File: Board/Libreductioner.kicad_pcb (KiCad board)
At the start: 2 copper layers, 50.2 x 73 mm, 46 parts, among them J1 Conn_01x02_Male, J2 Conn_01x02_Male, J3 Conn_01x02_Male, J4 Conn_01x02_Male, J5 Conn_01x02_Male, J6 Conn_01x02_Male, Q1 IRF3205, U1 ATMEGA168A-AU, U2 PC817, U3 PC817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

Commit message: Added gerber files for production
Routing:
- net VCC: track 147.9 -> 151.9 mm
- net GND: track 482.3 -> 480.1 mm
- net /RESET: track 53.6 -> 55.6 mm

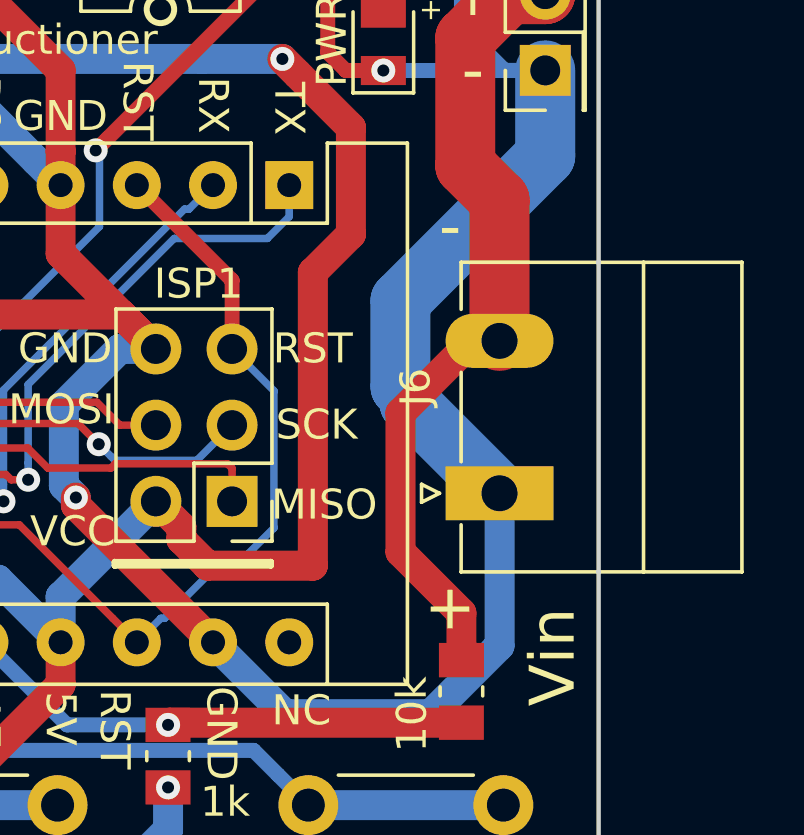
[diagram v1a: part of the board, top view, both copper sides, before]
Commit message: Fixed wrong description on Power Plug
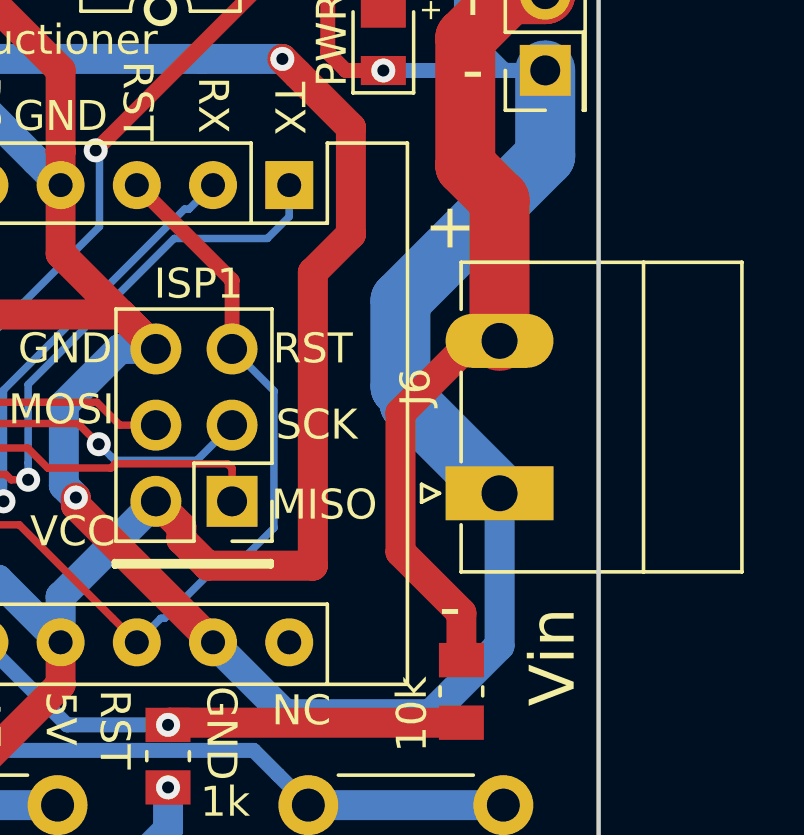
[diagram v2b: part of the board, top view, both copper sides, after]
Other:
- board text added: "Rev. 1.0.1 22.05.2018 Andreas Butti"
- board text removed: "Rev. 1.0 13.05.2018 Andreas Butti"
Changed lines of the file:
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@@
-(kicad_pcb (version 20171130) (host pcbnew 5.0.0-rc2-dev-unknown-f73b9a5~65~ubuntu16.04.1)
+(kicad_pcb (version 20171130) (host pcbnew 5.0.0-rc2-unknown-2d812c2~65~ubuntu16.04.1)
   (general
     (thickness 1.6)
@@
     (effects (font (size 0.8 0.8) (thickness 0.1)) (justify left))
   )
-  (gr_text "Rev. 1.0\n13.05.2018\nAndreas Butti" (at 89.535 79.756) (layer B.SilkS)
+  (gr_text "Rev. 1.0.1\n22.05.2018\nAndreas Butti" (at 89.535 79.756) (layer B.SilkS)
     (effects (font (size 1.5 1.5) (thickness 0.3)) (justify mirror))
   )
@@
   (gr_line (start 118.11 80.137) (end 118.11 70.104) (layer Edge.Cuts) (width 0.15))
   (gr_line (start 67.945 80.137) (end 67.945 67.945) (layer Edge.Cuts) (width 0.15))
-  (gr_text - (at 113.157 111.252) (layer F.SilkS)
+  (gr_text - (at 113.157 123.952) (layer F.SilkS)
     (effects (font (size 1.5 1.5) (thickness 0.3)))
   )
-  (gr_text + (at 113.157 123.952) (layer F.SilkS)
+  (gr_text + (at 113.157 111.252) (layer F.SilkS)
     (effects (font (size 1.5 1.5) (thickness 0.3)))
   )

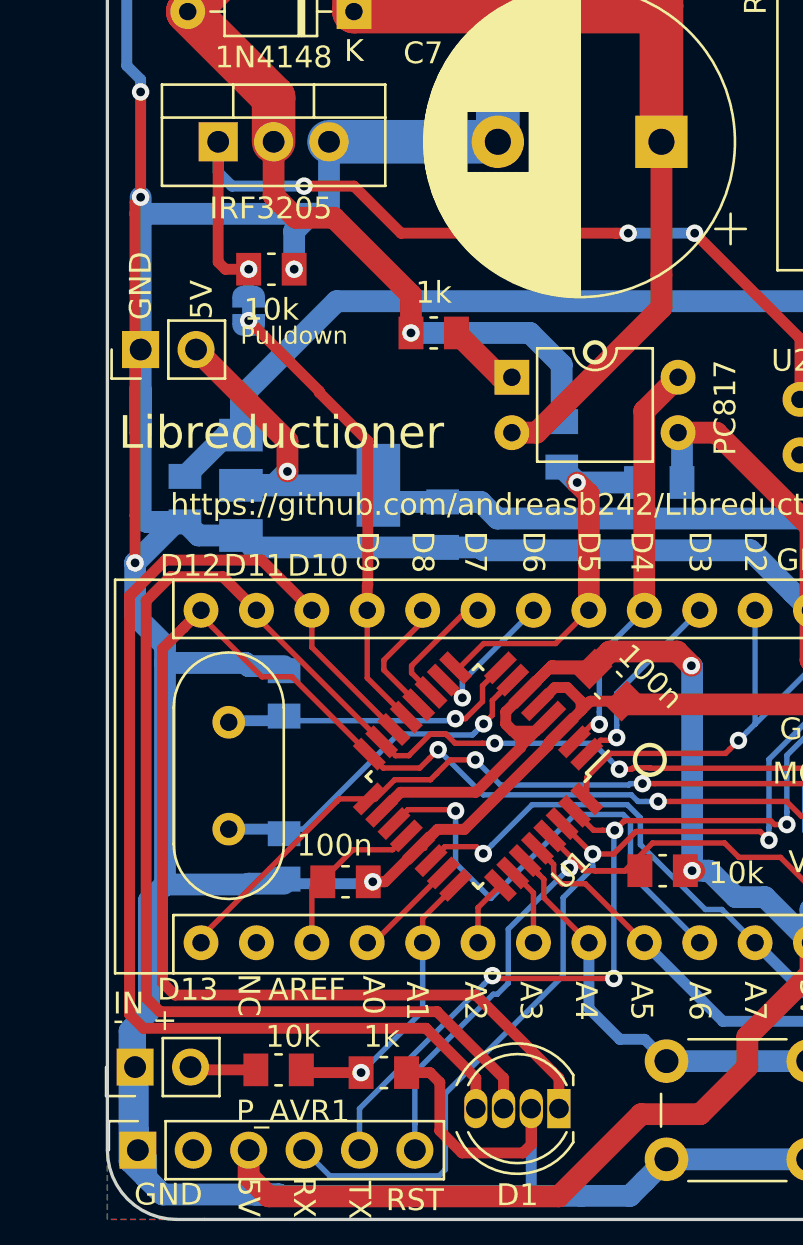
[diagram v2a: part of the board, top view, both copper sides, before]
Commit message: Fixed layout bugs found on Testing
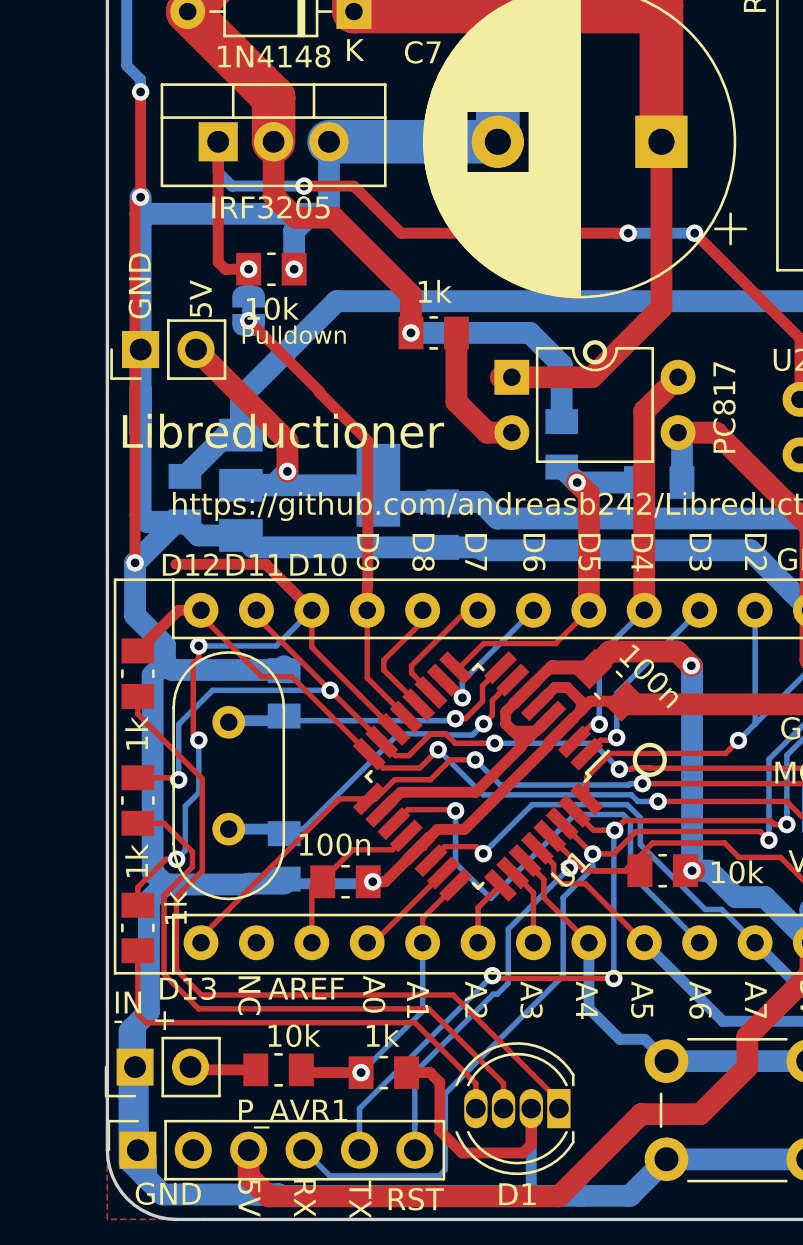
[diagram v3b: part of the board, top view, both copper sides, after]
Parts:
- added R16: 1k, Resistor_SMD:R_0805_2012Metric_Pad1.15x1.50mm_HandSolder, F.Cu at (69.3, 112.8)
- added R17: 1k, Resistor_SMD:R_0805_2012Metric_Pad1.15x1.50mm_HandSolder, F.Cu at (69.3, 118.6)
- added R18: 1k, Resistor_SMD:R_0805_2012Metric_Pad1.15x1.50mm_HandSolder, F.Cu at (69.3, 124.4)
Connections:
- D1 pad 1: /D12/MISO -> Net-(D1-Pad1)
- D1 pad 3: /D11/MOSI -> Net-(D1-Pad3)
- D1 pad 4: /D10 -> Net-(D1-Pad4)
- U3 pad 1: Net-(R5-Pad1) -> /BUFFERED12V
- U3 pad 2: /BUFFERED12V -> Net-(R5-Pad1)
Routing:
- net /D12/MISO: track 78.8 -> 43.3 mm
- net Net-(D1-Pad1): track 0.00 -> 34.6 mm
- net /D11/MOSI: track 76.6 -> 45.0 mm, vias 2 -> 4
- net Net-(D1-Pad3): track 0.00 -> 28.0 mm
- net /D10: track 54.9 -> 33.8 mm, vias 0 -> 3
- net Net-(D1-Pad4): track 0.00 -> 20.9 mm
- net Net-(R5-Pad1): track 3.38 -> 6.29 mm
- net GND: track 480.1 -> 480.7 mm
- net /BUFFERED12V: track 97.6 -> 97.1 mm

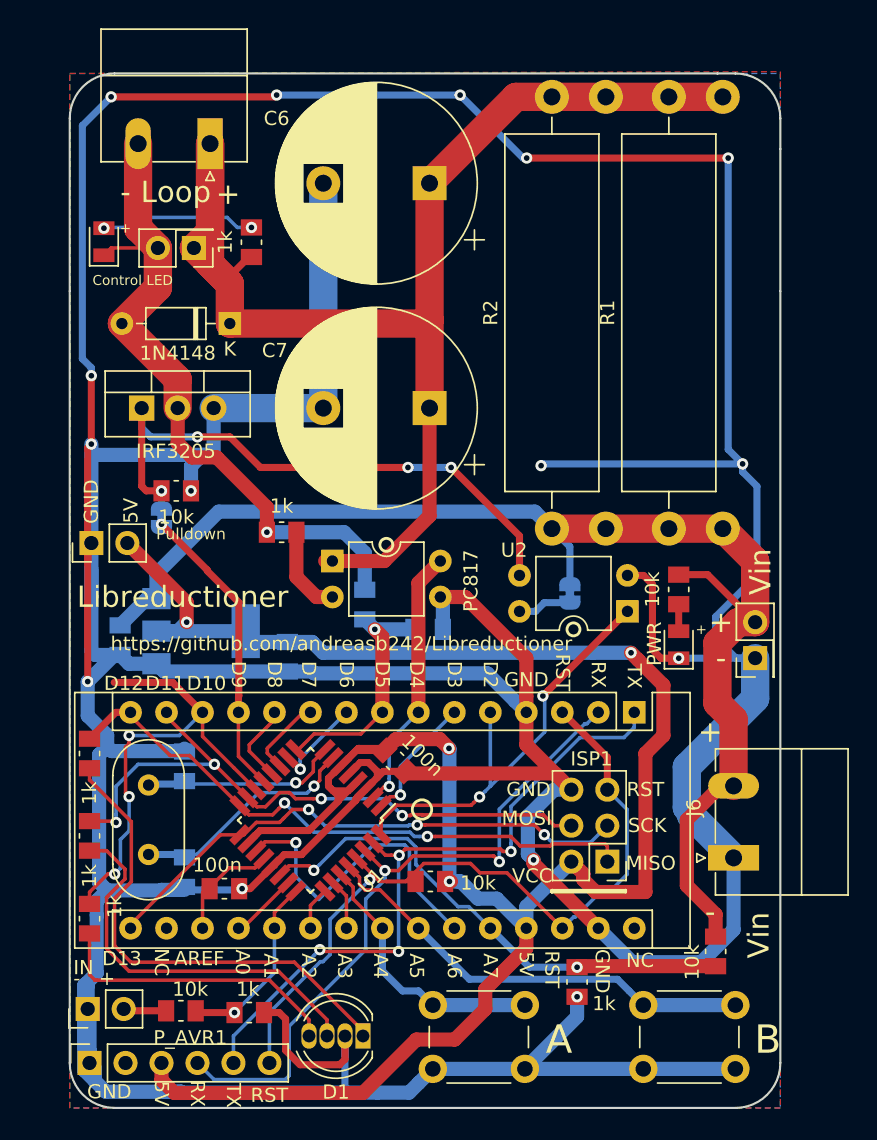
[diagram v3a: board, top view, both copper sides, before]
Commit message: Board Cleanup, removed all non-needed parts
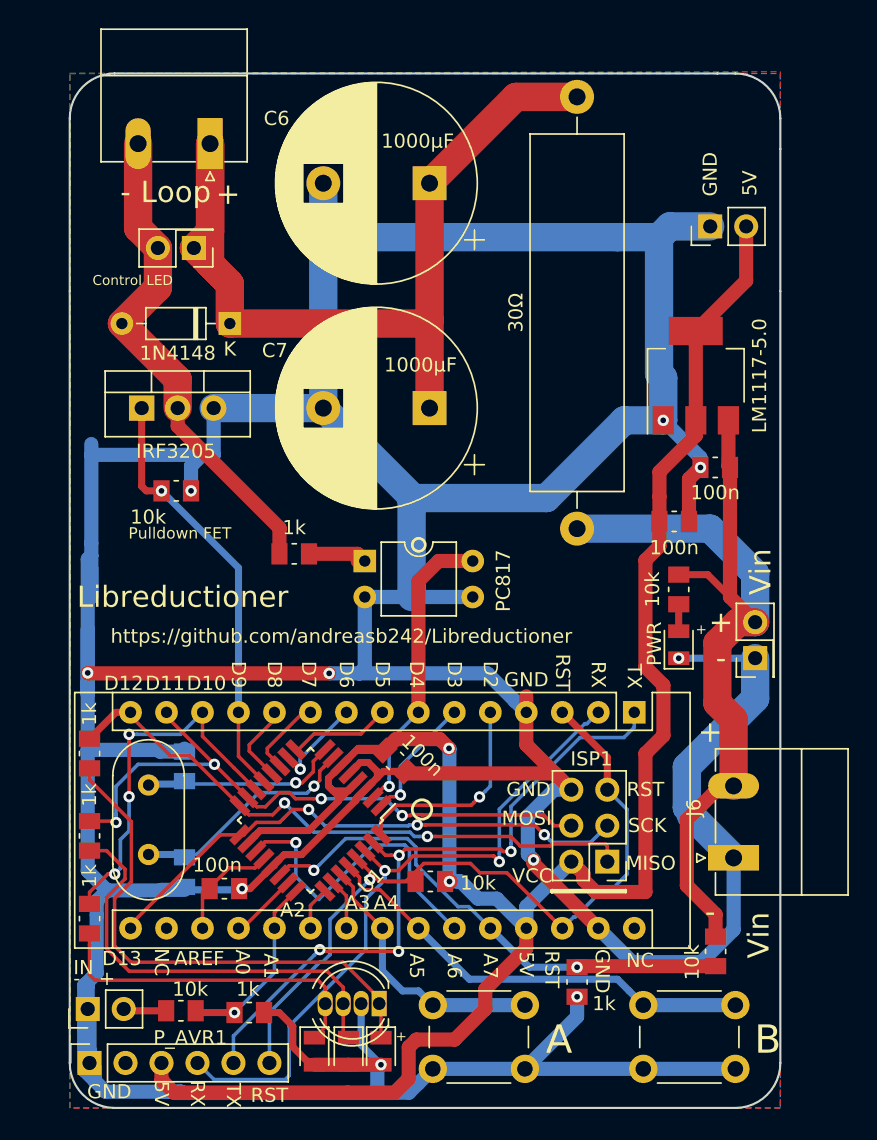
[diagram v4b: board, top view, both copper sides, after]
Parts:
- removed JP1, JP2: SolderJumper_2_Bridged, Jumper:SolderJumper-2_P1.3mm_Bridged_RoundedPad1.0x1.5mm
- removed R1, R2, R4: R, Resistor_THT:R_Axial_Power_L25.0mm_W6.4mm_P30.48mm
- removed R12, R13: R, Resistor_SMD:R_0805_2012Metric_Pad1.15x1.50mm_HandSolder
- removed R9: 1k, Resistor_SMD:R_0805_2012Metric_Pad1.15x1.50mm_HandSolder
- removed U2: PC817, Package_DIP:DIP-4_W7.62mm
- added D5: LED, LED_SMD:LED_0805_2012Metric_Pad0.97x1.50mm_HandSolder, F.Cu at (89.9, 133.8)
- added D6: LED, LED_SMD:LED_0805_2012Metric_Pad0.97x1.50mm_HandSolder, F.Cu at (87.6, 133.8)
- C6, C7: value CP -> 1000µF
- C8, C9, U4: moved to F.Cu
- R3: value R -> 30Ω; moved to F.Cu
- moved D3 59.0 mm to (85.2, 133.8), turned to 270 degrees
- moved J4 49.1 mm to (113.2, 75.6)
- moved C9 43.7 mm to (113.5, 92.6), turned to 180 degrees
- moved U4 39.3 mm to (112.1, 86.1), turned to 90 degrees
- moved C8 28.9 mm to (110.6, 96.4), turned to 0 degrees
- moved D1 2.56 mm to (89.8, 130.4)
- moved U3 2.29 mm to (88.8, 99.2)
- moved R3 2.03 mm to (103.8, 96.9)
- moved R5 1.76 mm to (83.8, 98.7)
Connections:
- D3 pad 1: Net-(D2-Pad2) -> Net-(D1-Pad4)
- D3 pad 2: Net-(D3-Pad2) -> GND
- Q1 pad 1: /FET_SIGNAL -> /D9
- R6 pad 1: /FET_SIGNAL -> /D9
- U3 pad 1: /BUFFERED12V -> Net-(R5-Pad1)
- U3 pad 2: Net-(R5-Pad1) -> GND
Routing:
- net GND: track 480.7 -> 426.1 mm, vias 15 -> 10
- net /FET_SIGNAL: track 42.3 -> 0.00 mm, vias 4 -> 0
- net /BUFFERED12V: track 97.1 -> 67.9 mm
- net +12V: track 94.5 -> 66.4 mm
- net /D2: track 31.4 -> 14.9 mm, vias 2 -> 1
- net Net-(D2-Pad2): track 48.5 -> 35.2 mm, vias 1 -> 0
- net Net-(D3-Pad2): track 11.0 -> 0.00 mm, vias 2 -> 0
- net VCC: track 151.9 -> 142.0 mm, vias 4 -> 2
- net /D5: track 17.0 -> 7.20 mm, vias 1 -> 0
- net /D9: track 21.2 -> 30.6 mm
- net /D10: track 33.8 -> 26.5 mm
- net /VFET: track 3.10 -> 0.00 mm
- net Net-(D1-Pad4): track 20.9 -> 23.9 mm
- net Net-(D1-Pad3): track 28.0 -> 30.7 mm
- net Net-(D1-Pad1): track 34.6 -> 37.3 mm
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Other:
- board text added: "Pulldown FET"
- board text added: "Rev. 1.1 27.05.2018 Andreas Butti"
- board text removed: "Pulldown"
- board text removed: "Rev. 1.0.1 22.05.2018 Andreas Butti"

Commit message: Removed Input: AVR is to slow for measuring the signal precise enough
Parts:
- removed J3: Conn_01x02_Male, Connector_PinHeader_2.54mm:PinHeader_1x02_P2.54mm_Vertical
- removed R14: 10k, Resistor_SMD:R_0805_2012Metric_Pad1.15x1.50mm_HandSolder
- removed R15: 1k, Resistor_SMD:R_0805_2012Metric_Pad1.15x1.50mm_HandSolder
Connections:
- A1 pad 17: (no net) -> Net-(A1-Pad17)
- A1 pad 30: (no net) -> Net-(A1-Pad30)
- P_AVR1 pad 2: (no net) -> Net-(P_AVR1-Pad2)
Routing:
- net GND: track 426.1 -> 415.1 mm
- net /A1: track 13.8 -> 3.90 mm, vias 1 -> 0
- net Net-(J3-Pad2): track 3.05 -> 0.00 mm
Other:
- board text removed: "- +"
